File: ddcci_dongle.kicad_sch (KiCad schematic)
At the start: 52 parts, among them U1 PCA9306, U10 TPD1E05U06DPY, U11 TPD1E05U06DPY, U12 TPD1E05U06DPY, U2 NCP1117-3.3_SOT223, U3 RP2040, U4 W25Q128JVPIQ, U6 TPD1E05U06DPY, U8 TPD1E05U06DPY, U9 TPD1E05U06DPY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

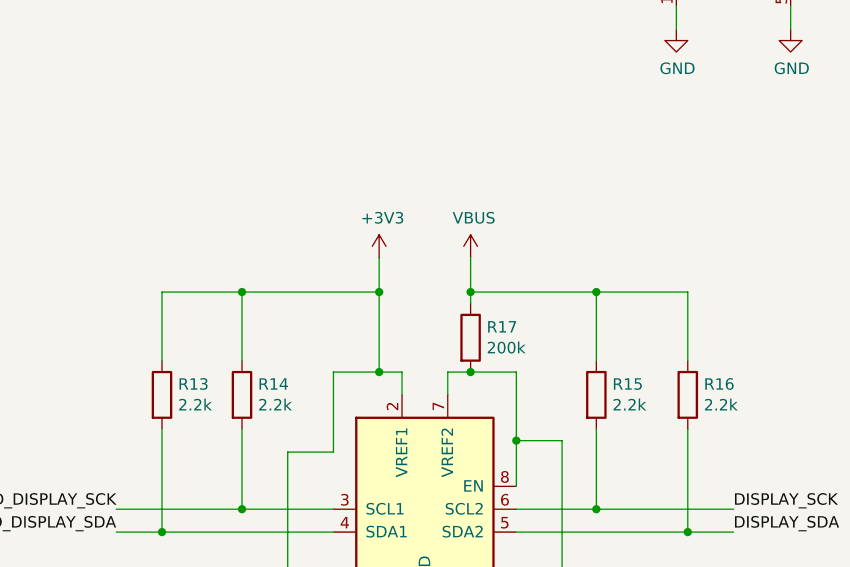
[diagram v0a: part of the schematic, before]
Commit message: Final update before rev1 production
* Update LCSC PN# fields
* Add ground to layer 3 (3.3v has been reduced to a polygon)
* Remove the antennas on the right (behind HDMI lanes)
* Remove the ground plane "capacitor" under the XTAL
* Prettier testpoint labels
* Prettier tracks overall

Signed-off-by: Elvira Khabirova <lineprinter0@gmail.com>
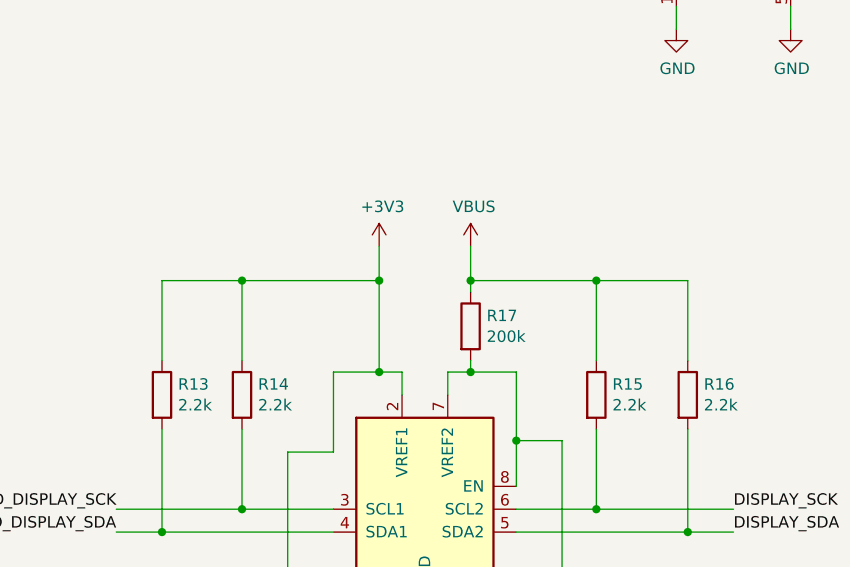
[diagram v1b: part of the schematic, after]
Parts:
- R13, R14, R15, R16: LCSC Part C98220 -> C25879
- R17: LCSC Part C2907238 -> C25764
- R18: LCSC Part C114622 -> C23178
- R7, R8: LCSC Part C60490 -> C25744
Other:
- moved on the sheet: R17
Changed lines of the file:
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@@
 	)
 	(junction
-		(at 236.22 199.39)
-		(diameter 0)
-		(color 0 0 0 0)
-	)
-	(junction
 		(at 77.47 223.52)
 		(diameter 0)
@@
 	)
 	(junction
-		(at 260.35 199.39)
-		(diameter 0)
-		(color 0 0 0 0)
-	)
-	(junction
 		(at 246.38 208.28)
 		(diameter 0)
@@
 	)
 	(junction
+		(at 260.35 198.12)
+		(diameter 0)
+		(color 0 0 0 0)
+	)
+	(junction
 		(at 283.21 53.34)
 		(diameter 0)
@@
 	)
 	(junction
-		(at 246.38 199.39)
+		(at 220.98 198.12)
 		(diameter 0)
 		(color 0 0 0 0)
@@
 	)
 	(junction
-		(at 220.98 199.39)
-		(diameter 0)
-		(color 0 0 0 0)
-	)
-	(junction
 		(at 220.98 223.52)
 		(diameter 0)
@@
 	)
 	(junction
+		(at 246.38 198.12)
+		(diameter 0)
+		(color 0 0 0 0)
+	)
+	(junction
 		(at 156.21 91.44)
 		(diameter 0)
@@
 	)
 	(junction
+		(at 236.22 198.12)
+		(diameter 0)
+		(color 0 0 0 0)
+	)
+	(junction
 		(at 123.19 212.09)
 		(diameter 0)
@@
 	(wire
 		(pts
+			(xy 246.38 198.12) (xy 246.38 199.39)
+		)
+		(stroke
+			(width 0)
+			(type default)
+		)
+	)
+	(wire
+		(pts
 			(xy 320.04 68.58) (xy 325.12 68.58)
 		)
@@
 	(wire
 		(pts
-			(xy 212.09 199.39) (xy 220.98 199.39)
+			(xy 212.09 198.12) (xy 220.98 198.12)
 		)
 		(stroke
@@
 	(wire
 		(pts
-			(xy 260.35 199.39) (xy 270.51 199.39)
+			(xy 260.35 198.12) (xy 270.51 198.12)
 		)
 		(stroke
@@
 	(wire
 		(pts
-			(xy 236.22 199.39) (xy 236.22 208.28)
-		)
-		(stroke
-			(width 0)
-			(type default)
-		)
-	)
-	(wire
-		(pts
 			(xy 83.82 41.91) (xy 74.93 41.91)
 		)
@@
 	(wire
 		(pts
+			(xy 246.38 207.01) (xy 246.38 208.28)
+		)
+		(stroke
+			(width 0)
+			(type default)
+		)
+	)
+	(wire
+		(pts
 			(xy 370.84 35.56) (xy 370.84 33.02)
 		)
@@
 	(wire
 		(pts
-			(xy 273.05 27.94) (xy 273.05 66.04)
+			(xy 236.22 198.12) (xy 236.22 208.28)
 		)
 		(stroke
@@
 	(wire
 		(pts
-			(xy 57.15 184.15) (xy 123.19 184.15)
+			(xy 273.05 27.94) (xy 273.05 66.04)
 		)
 		(stroke
@@
 	(wire
 		(pts
-			(xy 250.19 100.33) (xy 236.22 100.33)
+			(xy 57.15 184.15) (xy 123.19 184.15)
 		)
 		(stroke
@@
 	(wire
 		(pts
-			(xy 260.35 199.39) (xy 260.35 207.01)
+			(xy 250.19 100.33) (xy 236.22 100.33)
 		)
 		(stroke
@@
 	(wire
 		(pts
-			(xy 246.38 200.66) (xy 246.38 199.39)
-		)
-		(stroke
-			(width 0)
-			(type default)
-		)
-	)
-	(wire
-		(pts
 			(xy 238.76 208.28) (xy 238.76 210.82)
 		)
@@
 	(wire
 		(pts
-			(xy 246.38 199.39) (xy 246.38 195.58)
+			(xy 246.38 198.12) (xy 246.38 194.31)
 		)
 		(stroke
@@
 	(wire
 		(pts
-			(xy 246.38 199.39) (xy 260.35 199.39)
+			(xy 246.38 198.12) (xy 260.35 198.12)
 		)
 		(stroke
@@
 	(wire
 		(pts
-			(xy 220.98 199.39) (xy 236.22 199.39)
+			(xy 220.98 198.12) (xy 236.22 198.12)
 		)
 		(stroke
@@
 	(wire
 		(pts
+			(xy 236.22 198.12) (xy 236.22 194.31)
+		)
+		(stroke
+			(width 0)
+			(type default)
+		)
+	)
+	(wire
+		(pts
 			(xy 52.07 22.86) (xy 62.23 22.86)
 		)
@@
 	(wire
 		(pts
+			(xy 260.35 198.12) (xy 260.35 207.01)
+		)
+		(stroke
+			(width 0)
+			(type default)
+		)
+	)
+	(wire
+		(pts
 			(xy 236.22 91.44) (xy 250.19 91.44)
 		)
@@
 	(wire
 		(pts
-			(xy 212.09 207.01) (xy 212.09 199.39)
+			(xy 212.09 207.01) (xy 212.09 198.12)
 		)
 		(stroke
@@
 	(wire
 		(pts
-			(xy 236.22 199.39) (xy 236.22 195.58)
-		)
-		(stroke
-			(width 0)
-			(type default)
-		)
-	)
-	(wire
-		(pts
 			(xy 44.45 44.45) (xy 52.07 44.45)
 		)
@@
 	(wire
 		(pts
-			(xy 270.51 207.01) (xy 270.51 199.39)
+			(xy 270.51 207.01) (xy 270.51 198.12)
 		)
 		(stroke
@@
 	(wire
 		(pts
-			(xy 220.98 199.39) (xy 220.98 207.01)
+			(xy 220.98 198.12) (xy 220.98 207.01)
 		)
 		(stroke
@@
 	(symbol
 		(lib_id "Device:R")
-		(at 246.38 204.47 0)
+		(at 246.38 203.2 0)
 		(unit 1)
 		(exclude_from_sim no)
@@
 		(dnp no)
 		(property "Reference" "R17"
-			(at 248.158 203.3016 0)
+			(at 248.158 202.0316 0)
 			(effects
 				(font
@@
 		)
 		(property "Value" "200k"
-			(at 248.158 205.613 0)
+			(at 248.158 204.343 0)
 			(effects
 				(font
@@
 		)
 		(property "Footprint" "Resistor_SMD:R_0402_1005Metric"
-			(at 244.602 204.47 90)
+			(at 244.602 203.2 90)
 			(effects
 				(font
@@
 		)
 		(property "Datasheet" "~"
-			(at 246.38 204.47 0)
+			(at 246.38 203.2 0)
 			(effects
 				(font
@@
 		)
 		(property "Description" ""
-			(at 246.38 204.47 0)
+			(at 246.38 203.2 0)
 			(effects
 				(font
@@
 			)
 		)
-		(property "LCSC Part" "C2907238"
-			(at 246.38 204.47 0)
+		(property "LCSC Part" "C25764"
+			(at 246.38 203.2 0)
 			(effects
 				(font
@@
 			)
 		)
-		(property "LCSC Part" "C114622"
+		(property "LCSC Part" "C23178"
 			(at 226.06 236.22 0)
 			(effects
@@
 			)
 		)
-		(property "LCSC Part" "C98220"
+		(property "LCSC Part" "C25879"
 			(at 212.09 210.82 0)
 			(effects
@@
 			)
 		)
-		(property "LCSC Part" "C98220"
+		(property "LCSC Part" "C25879"
 			(at 270.51 210.82 0)
 			(effects
@@
 			)
 		)
-		(property "LCSC Part" "C60490"
+		(property "LCSC Part" "C25744"
 			(at 245.11 137.16 90)
 			(effects
@@
 			)
 		)
-		(property "LCSC Part" "C60490"
+		(property "LCSC Part" "C25744"
 			(at 121.92 105.41 0)
 			(effects
@@
 			)
 		)
-		(property "LCSC Part" "C98220"
+		(property "LCSC Part" "C25879"
 			(at 220.98 210.82 0)
 			(effects
@@
 	(symbol
 		(lib_id "power:+3V3")
-		(at 236.22 195.58 0)
+		(at 236.22 194.31 0)
 		(unit 1)
 		(exclude_from_sim no)
@@
 		(dnp no)
 		(property "Reference" "#PWR032"
-			(at 236.22 199.39 0)
+			(at 236.22 198.12 0)
 			(effects
 				(font
@@
 		)
 		(property "Value" "+3V3"
-			(at 236.601 191.1858 0)
+			(at 236.601 189.9158 0)
 			(effects
 				(font
@@
 		)
 		(property "Footprint" ""
-			(at 236.22 195.58 0)
+			(at 236.22 194.31 0)
 			(effects
 				(font
@@
 		)
 		(property "Datasheet" ""
-			(at 236.22 195.58 0)
+			(at 236.22 194.31 0)
 			(effects
 				(font
@@
 		)
 		(property "Description" ""
-			(at 236.22 195.58 0)
+			(at 236.22 194.31 0)
 			(effects
 				(font
@@
 	(symbol
 		(lib_id "power:VBUS")
-		(at 246.38 195.58 0)
+		(at 246.38 194.31 0)
 		(unit 1)
 		(exclude_from_sim no)
@@
 		(dnp no)
 		(property "Reference" "#PWR033"
-			(at 246.38 199.39 0)
+			(at 246.38 198.12 0)
 			(effects
 				(font
@@
 		)
 		(property "Value" "VBUS"
-			(at 246.761 191.1858 0)
+			(at 246.761 189.9158 0)
 			(effects
 				(font
@@
 		)
 		(property "Footprint" ""
-			(at 246.38 195.58 0)
+			(at 246.38 194.31 0)
 			(effects
 				(font
@@
 		)
 		(property "Datasheet" ""
-			(at 246.38 195.58 0)
+			(at 246.38 194.31 0)
 			(effects
 				(font
@@
 		)
 		(property "Description" ""
-			(at 246.38 195.58 0)
+			(at 246.38 194.31 0)
 			(effects
 				(font
@@
 			)
 		)
-		(property "LCSC Part" "C98220"
+		(property "LCSC Part" "C25879"
 			(at 260.35 210.82 0)
 			(effects

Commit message: Fix SDA/SCL for the monitor. Bump to rev2
Signed-off-by: Elvira Khabirova <lineprinter0@gmail.com>
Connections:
- net DISPLAY_SCK: now also HDMI1.15 (SCL), U5.15 (I2C-CLK), U9.1 (I/O); no longer HDMI1.16 (SDA), U5.16 (I2C_DATA), U8.1 (I/O)
- net DISPLAY_SDA: now also HDMI1.16 (SDA), U5.16 (I2C_DATA), U8.1 (I/O); no longer HDMI1.15 (SCL), U5.15 (I2C-CLK), U9.1 (I/O)
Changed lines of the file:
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@@
-		)
-	)
-	(label "DISPLAY_SCK"
-		(at 109.22 240.03 0)
-		(effects
-			(font
-				(size 1.27 1.27)
-			)
-			(justify left bottom)
 		)
 	)
@@
 		)
 	)
+	(label "DISPLAY_SCK"
+		(at 109.22 261.62 0)
+		(effects
+			(font
+				(size 1.27 1.27)
+			)
+			(justify left bottom)
+		)
+	)
 	(label "PERIPHERAL_SDA"
 		(at 355.6 180.34 180)
@@
 		)
 	)
+	(label "DISPLAY_SDA"
+		(at 109.22 240.03 0)
+		(effects
+			(font
+				(size 1.27 1.27)
+			)
+			(justify left bottom)
+		)
+	)
 	(label "QSPI_SD0"
 		(at 236.22 88.9 0)
@@
 		(effects
 			(font
-				(size 1.27 1.27)
-			)
-			(justify left bottom)
-		)
-	)
-	(label "DISPLAY_SDA"
-		(at 109.22 261.62 0)
-		(effects
-			(font

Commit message: Make the board shorter for rev2
Signed-off-by: Elvira Khabirova <lineprinter0@gmail.com>
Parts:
- removed U2: NCP1117-3.3_SOT223, Package_TO_SOT_SMD:SOT-223-3_TabPin2, symbol Regulator_Linear:NCP1117-3.3_SOT223
- added U7: ~, ddcci_dongle_parts:XDFN-8_L1.6-W1.2-P0.40-BL-EP, symbol ddcci_dongle_parts:NCP186AMX330TAG
- C19, C5: value 10uF -> 1uF X5R/X7R; LCSC Part C15850 -> C28323
- CN1: footprint ddcci_dongle_parts:AUDIO-SMD_PJ-320D-1 -> ddcci_dongle_parts:AUDIO-TH_PJ-320A-4P-DIP; symbol ddcci_dongle_parts:PJ-320D -> ddcci_dongle_parts:PJ-320A-4P DIP; LCSC Part Name PJ-320D贴片 编带 -> 3.5mm耳机座; Manufacturer Part PJ-320D -> PJ-320A-4P DIP; Supplier Part C431535 -> C18185602
- H1: footprint MountingHole:MountingHole_2.7mm_M2.5_Pad -> MountingHole:MountingHole_2.2mm_M2_Pad
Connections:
- net +3V3: now also CN1.A, U7.1 (OUT), U7.2 (OUT), U7.4 (FB/ADJ); no longer CN1.1
- net GND: now also CN1.D, U7.3 (NC), U7.5 (GND), U7.9 (EP); no longer CN1.4
- net PERIPHERAL_SCK: now also CN1.B; no longer CN1.2
- net PERIPHERAL_SDA: now also CN1.C; no longer CN1.3
- net VBUS: now also U7.6 (EN), U7.7 (IN), U7.8 (IN)
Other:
- moved on the sheet: C19, C5, CN1

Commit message: Make the board even shorter
Signed-off-by: Elvira Khabirova <lineprinter0@gmail.com>
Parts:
- TPBOOT1, TPCLK1, TPGND1, TPSWD1: footprint TestPoint:TestPoint_Pad_D2.0mm -> TestPoint:TestPoint_Pad_D1.5mm
- U4: value W25Q128JVPIQ -> W25Q16JVUXIQ; footprint Package_SON:WSON-8-1EP_6x5mm_P1.27mm_EP3.4x4.3mm -> Package_SON:Winbond_USON-8-1EP_3x2mm_P0.5mm_EP0.2x1.6mm; LCSC Part C190862 -> C2843335
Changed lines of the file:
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@@
 			)
 		)
-		(property "Footprint" "TestPoint:TestPoint_Pad_D2.0mm"
+		(property "Footprint" "TestPoint:TestPoint_Pad_D1.5mm"
 			(at 80.01 113.03 0)
 			(effects
@@
 			)
 		)
-		(property "Footprint" "TestPoint:TestPoint_Pad_D2.0mm"
+		(property "Footprint" "TestPoint:TestPoint_Pad_D1.5mm"
 			(at 227.33 146.05 0)
 			(effects
@@
 			)
 		)
-		(property "Footprint" "TestPoint:TestPoint_Pad_D2.0mm"
+		(property "Footprint" "TestPoint:TestPoint_Pad_D1.5mm"
 			(at 236.22 143.51 0)
 			(effects
@@
 			)
 		)
-		(property "Value" "W25Q128JVPIQ"
+		(property "Value" "W25Q16JVUXIQ"
 			(at 168.148 135.382 0)
 			(effects
@@
 			)
 		)
-		(property "Footprint" "Package_SON:WSON-8-1EP_6x5mm_P1.27mm_EP3.4x4.3mm"
+		(property "Footprint" "Package_SON:Winbond_USON-8-1EP_3x2mm_P0.5mm_EP0.2x1.6mm"
 			(at 156.21 100.33 0)
 			(effects
@@
 			)
 		)
-		(property "Datasheet" "https://www.winbond.com/resource-files/w25q128jv_dtr%20revc%2003272018%20plus.pdf"
+		(property "Datasheet" ""
 			(at 156.21 97.79 0)
 			(effects
@@
 			)
 		)
-		(property "LCSC Part" "C190862"
+		(property "LCSC Part" "C2843335"
 			(at 156.21 123.19 0)
 			(effects
@@
 			)
 		)
-		(property "Footprint" "TestPoint:TestPoint_Pad_D2.0mm"
+		(property "Footprint" "TestPoint:TestPoint_Pad_D1.5mm"
 			(at 87.63 110.49 0)
 			(effects

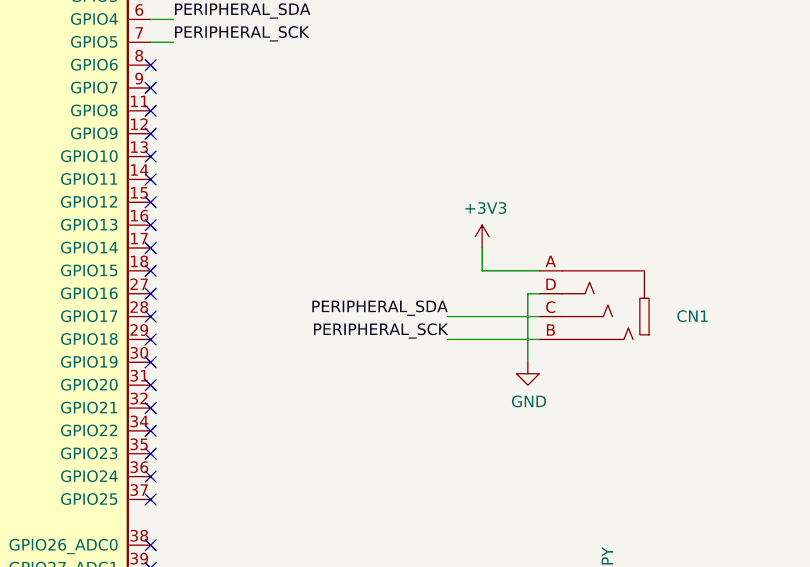
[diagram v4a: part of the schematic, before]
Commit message: Change pinout of the TRRS jack
This way the board won't burn if a TRS cable is plugged in.

Signed-off-by: Elvira Khabirova <lineprinter0@gmail.com>
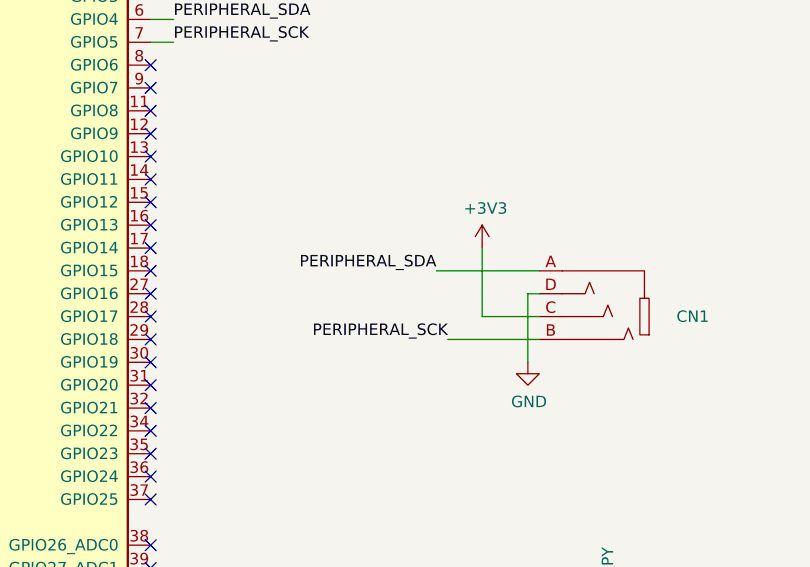
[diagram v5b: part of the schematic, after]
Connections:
- net +3V3: now also CN1.C; no longer CN1.A
- net PERIPHERAL_SDA: now also CN1.A; no longer CN1.C
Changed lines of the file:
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@@
+	(wire
+		(pts
+			(xy 350.52 127) (xy 356.87 127)
+		)
+		(stroke
+			(width 0)
+			(type default)
+		)
+	)
 	(wire
 		(pts
@@
 	(wire
 		(pts
-			(xy 350.52 121.92) (xy 350.52 119.38)
-		)
-		(stroke
-			(width 0)
-			(type default)
-		)
-	)
-	(wire
-		(pts
 			(xy 77.47 223.52) (xy 77.47 228.6)
 		)
@@
 	(wire
 		(pts
-			(xy 346.71 127) (xy 356.87 127)
-		)
-		(stroke
-			(width 0)
-			(type default)
-		)
-	)
-	(wire
-		(pts
 			(xy 212.09 125.73) (xy 212.09 127)
 		)
@@
 	(wire
 		(pts
+			(xy 350.52 119.38) (xy 350.52 127)
+		)
+		(stroke
+			(width 0)
+			(type default)
+		)
+	)
+	(wire
+		(pts
 			(xy 74.93 34.29) (xy 74.93 27.94)
 		)
@@
 	(wire
 		(pts
-			(xy 350.52 121.92) (xy 356.87 121.92)
+			(xy 345.44 121.92) (xy 356.87 121.92)
 		)
 		(stroke
@@
 	)
 	(label "PERIPHERAL_SDA"
-		(at 346.71 127 180)
+		(at 345.44 121.92 180)
 		(effects
 			(font
